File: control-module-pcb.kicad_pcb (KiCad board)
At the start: 4 copper layers, 59 x 75 mm, 79 parts, among them J1 Programming Header, J2 Programming Jumper, J3 Power Outputs, J4 Ignition Outputs, J5 Power Input, SW1 EN, U1 ESP32-S3-WROOM-1, U10 ITS4200SSJDXUMA1, U11 ITS4200SSJDXUMA1, U12 ITS4200SSJDXUMA1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

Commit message: layout mostly complete
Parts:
- added REF**: MountingHole_3.2mm_M3_ISO7380_Pad_TopBottom, MountingHole:MountingHole_3.2mm_M3_ISO7380_Pad_TopBottom, F.Cu at (171.5, 122.5)
- added REF**: MountingHole_3.2mm_M3_ISO7380_Pad_TopBottom, MountingHole:MountingHole_3.2mm_M3_ISO7380_Pad_TopBottom, F.Cu at (171.8, 64.5)
- moved R23 52.5 mm to (173.8, 77.1), turned to 180 degrees
- moved R24 52.2 mm to (173.8, 78.8)
- moved R25 51.9 mm to (173.8, 80.5), turned to 180 degrees
- moved R26 51.6 mm to (173.8, 82.2)
- moved J5 49.8 mm to (146.4, 128.6), turned to 90 degrees
- moved R2 31.6 mm to (145.3, 92.8), turned to 0 degrees
- moved SW1 27.6 mm to (162.8, 61.7), turned to -90 degrees
- moved J1 26.4 mm to (152.2, 67.1), turned to 90 degrees
- moved J2 18.8 mm to (144.7, 67.1), turned to 90 degrees
- moved U1 17.4 mm to (151.4, 82.1), turned to 90 degrees
- moved C2 7.39 mm to (146.9, 113.3), turned to 0 degrees
- moved C1A1 4.25 mm to (150.7, 108.4)
- moved C1B1 4.25 mm to (163.8, 108.3)
- moved C1C1 4.25 mm to (152.8, 108.3)
- moved C1D1 4.25 mm to (161.8, 108.2)
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- renumbered R25 to R24, R24 to R25
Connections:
- R23 pad 2: Net-(U1-GPIO1/TOUCH1/ADC1_CH0) -> Net-(U1-GPIO6/TOUCH6/ADC1_CH5)
- R24 pad 1: Net-(U1-GPIO1/TOUCH1/ADC1_CH0) -> Net-(U1-GPIO6/TOUCH6/ADC1_CH5)
- R25 pad 2: Net-(U1-GPIO2/TOUCH2/ADC1_CH1) -> Net-(U1-GPIO7/TOUCH7/ADC1_CH6)
- R26 pad 1: Net-(U1-GPIO2/TOUCH2/ADC1_CH1) -> Net-(U1-GPIO7/TOUCH7/ADC1_CH6)
- U1 pad 10: /R_BLIND_SPOT_ERR -> unconnected-(U1-GPIO17/U1TXD/ADC2_CH6-Pad10)
- U1 pad 11: /DASH_CAM_ERR -> /BACKUP_CAM_EN
- U1 pad 12: /HEAD_UNIT_EN -> /BACK_UP_CAM_ERR
- U1 pad 15: /IGNITION1_EN -> /DASH_CAM_EN
- U1 pad 16: /ACCESSORY1_ERR -> /DASH_CAM_ERR
- U1 pad 17: /L_BLIND_SPOT_EN -> /R_BLIND_SPOT_EN
- U1 pad 18: /R_BLIND_SPOT_EN -> /R_BLIND_SPOT_ERR
- U1 pad 19: /DASH_CAM_EN -> /L_BLIND_SPOT_EN
- U1 pad 20: /BACKUP_CAM_EN -> /L_BLIND_SPOT_ERR
- U1 pad 21: /HEAD_UNIT_ERR -> /HEAD_UNIT_EN
- U1 pad 22: /L_BLIND_SPOT_ERR -> /HEAD_UNIT_ERR
- U1 pad 23: /BACK_UP_CAM_ERR -> /STARTER_ERR
- U1 pad 24: /IGNITION2_ERR -> /STARTER_EN
- U1 pad 26: /IGNITION1_ERR -> /ACCESSORY2_EN
- U1 pad 28: unconnected-(U1-SPIIO6/GPIO35/FSPID/SUBSPID-Pad28) -> /IGNITION2_ERR
- U1 pad 29: unconnected-(U1-SPIIO7/GPIO36/FSPICLK/SUBSPICLK-Pad29) -> /IGNITION2_EN
- U1 pad 30: unconnected-(U1-SPIDQS/GPIO37/FSPIQ/SUBSPIQ-Pad30) -> /ACCESSORY1_ERR
- U1 pad 31: /STARTER_ERR -> /ACCESSORY1_EN
- U1 pad 38: Net-(U1-GPIO2/TOUCH2/ADC1_CH1) -> /IGNITION1_ERR
- U1 pad 39: Net-(U1-GPIO1/TOUCH1/ADC1_CH0) -> /IGNITION1_EN
- U1 pad 4: /ACCESSORY1_EN -> unconnected-(U1-GPIO4/TOUCH4/ADC1_CH3-Pad4)
- U1 pad 5: /IGNITION2_EN -> unconnected-(U1-GPIO5/TOUCH5/ADC1_CH4-Pad5)
- U1 pad 6: /ACCESSORY2_EN -> Net-(U1-GPIO6/TOUCH6/ADC1_CH5)
- U1 pad 7: /STARTER -> Net-(U1-GPIO7/TOUCH7/ADC1_CH6)
- U5 pad 3: /R_BLIND_SPOT_EN -> /L_BLIND_SPOT_EN
- U6 pad 3: /DASH_CAM_EN -> /R_BLIND_SPOT_EN
- U7 pad 3: /L_BLIND_SPOT_EN -> /DASH_CAM_EN
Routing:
- net /5V: track 52.1 -> 150.1 mm, vias 8 -> 24
- net /DASH_CAM_SHUTDOWN: track 0.00 -> 54.7 mm, vias 0 -> 2
- net /BACKUP_CAM_EN: track 0.00 -> 54.2 mm
- net /EN: track 0.00 -> 46.8 mm, vias 0 -> 2
- net /BACK_UP_CAM_ERR: track 5.95 -> 52.0 mm
- net /HEAD_UNIT_SHUTDOWN: track 0.00 -> 45.7 mm, vias 0 -> 2
- net /IGNITION1_EN: track 0.00 -> 44.7 mm
- net /DASH_CAM_EN: track 0.00 -> 43.8 mm
- net /IGNITION1_ERR: track 0.00 -> 40.8 mm
- net /DASH_CAM_ERR: track 5.93 -> 45.8 mm
- net /R_BLIND_SPOT_EN: track 0.00 -> 38.3 mm
- net /R_BLIND_SPOT_ERR: track 5.93 -> 40.0 mm
- net /L_BLIND_SPOT_EN: track 0.00 -> 32.4 mm
- net Net-(U1-GPIO6/TOUCH6/ADC1_CH5): track 0.00 -> 30.7 mm, vias 0 -> 2
- net /ACCESSORY1_EN: track 0.00 -> 29.3 mm
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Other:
- board size 59 x 75 mm -> 59 x 75.9 mm

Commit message: made a few adjustments and generated gerbers
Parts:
- moved C7 0.31 mm to (178.3, 93.7)
- moved C9 0.25 mm to (178.3, 102.0)
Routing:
- net /5V: track 150.1 -> 150.2 mm, vias 24 -> 26
- added copper zone on B.Cu, net GND
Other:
- board size 59 x 75.9 mm -> 58.2 x 75.9 mm
- board text added: "Ben Martens 2024-02"

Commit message: add LED for debugging
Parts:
- added D1: LED, LED_SMD:LED_0603_1608Metric, F.Cu at (168.6, 100.2)
- added R27: 220, Resistor_SMD:R_0603_1608Metric, F.Cu at (168.6, 98.4)
- R8: value 115 -> 145
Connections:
- U1 pad 5: unconnected-(U1-GPIO5/TOUCH5/ADC1_CH4-Pad5) -> Net-(U1-GPIO5/TOUCH5/ADC1_CH4)
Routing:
- net Net-(U1-GPIO5/TOUCH5/ADC1_CH4): track 0.00 -> 22.8 mm, vias 0 -> 2
- net Net-(D1-A): track 0.00 -> 1.76 mm
- net GND: vias 68 -> 69

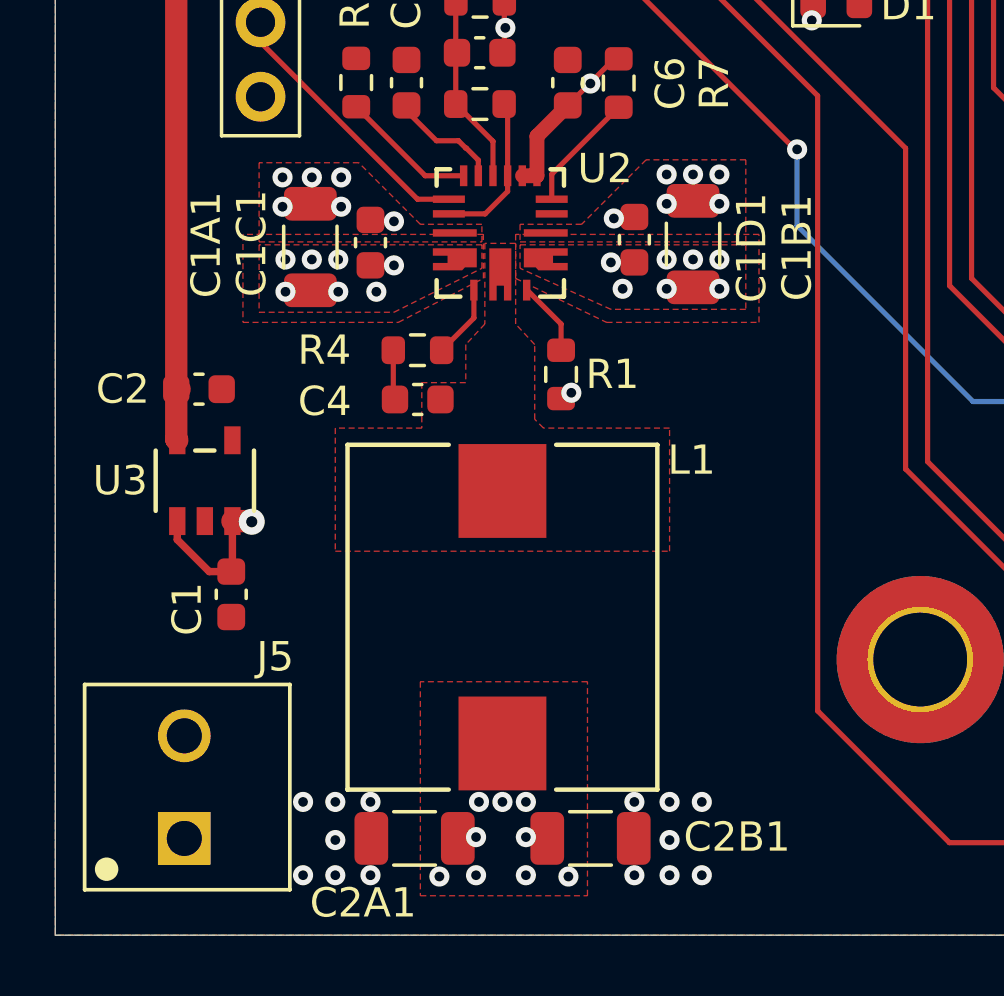
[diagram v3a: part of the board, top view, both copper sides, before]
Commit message: a few silk screen updates
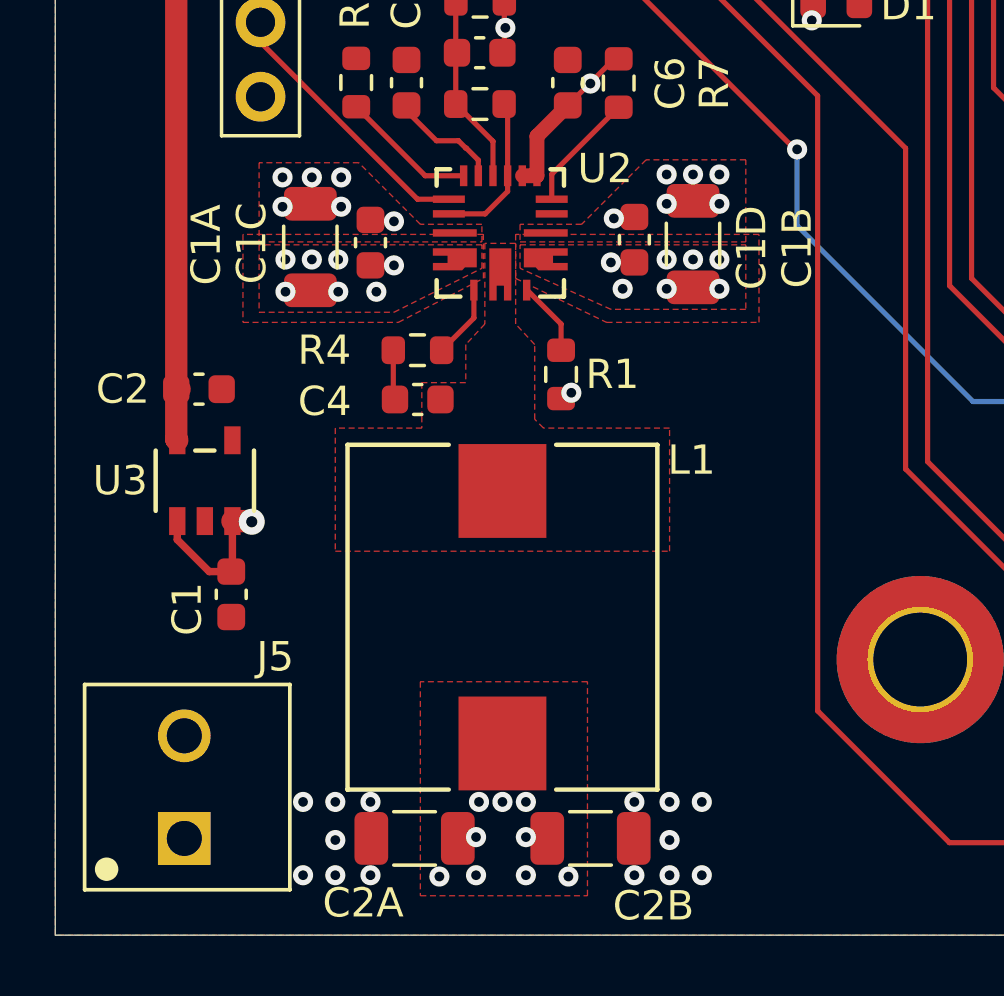
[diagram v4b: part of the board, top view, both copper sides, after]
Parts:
- renumbered C1A1 to C1A, C1B1 to C1B, C1C1 to C1C, C1D1 to C1D, C2A1 to C2A, C2B1 to C2B
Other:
- board text added: "Ben Martens 2024-02 Control Module v1"
- board text removed: "Ben Martens 2024-02"
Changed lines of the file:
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@@
         (effects (font (size 1 1) (thickness 0.15)))
     )
-    (fp_text value "4.7u" (at 0 0 90 unlocked) (layer "F.Fab")
+    (fp_text value "4.7u" (at -0.9447 6.25 90 unlocked) (layer "F.Fab")
         (effects (font (size 1 1) (thickness 0.15)))
     )
@@
     (zone_connect 2)
     (attr smd exclude_from_pos_files)
-    (fp_text reference "C2B1" (at 4.996867 -0.044389) (layer "F.SilkS")
+    (fp_text reference "C2B" (at 2.146867 2.300311) (layer "F.SilkS")
         (effects (font (size 1 1) (thickness 0.15)))
     )
@@
         (effects (font (size 1 1) (thickness 0.15)))
     )
-    (fp_text value "Programming Jumper" (at 8.525 4.975 90) (layer "F.Fab")
+    (fp_text value "Programming Jumper" (at 18.825 3.975 90) (layer "F.Fab")
         (effects (font (size 1 1) (thickness 0.15)))
     )
@@
     (property "ki_keywords" "cap capacitor")
     (attr smd exclude_from_pos_files)
-    (fp_text reference "C1B1" (at 0.125126 -3.551002 90) (layer "F.SilkS")
+    (fp_text reference "C1B" (at 0.125126 -3.551002 90) (layer "F.SilkS")
         (effects (font (size 1 1) (thickness 0.15)))
     )
@@
     (zone_connect 2)
     (attr smd exclude_from_pos_files)
-    (fp_text reference "C2A1" (at 1.753133 -2.200311 180) (layer "F.SilkS")
+    (fp_text reference "C2A" (at 1.753133 -2.200311 180) (layer "F.SilkS")
         (effects (font (size 1 1) (thickness 0.15)))
     )
@@
     (property "ki_keywords" "cap capacitor")
     (attr smd)
-    (fp_text reference "C1D1" (at 0.275 -4 90) (layer "F.SilkS")
+    (fp_text reference "C1D" (at 0.275 -4 90) (layer "F.SilkS")
         (effects (font (size 1 1) (thickness 0.15)))
     )
@@
         (effects (font (size 1 1) (thickness 0.15)))
     )
-    (fp_text value "Programming Header" (at 8.425 7.53 90) (layer "F.Fab")
+    (fp_text value "Programming Header" (at 18.625 6.23 90) (layer "F.Fab")
         (effects (font (size 1 1) (thickness 0.15)))
     )
@@
     (property "ki_keywords" "cap capacitor")
     (attr smd)
-    (fp_text reference "C1C1" (at 0.024874 4.051002 90) (layer "F.SilkS")
+    (fp_text reference "C1C" (at 0.024874 4.051002 90) (layer "F.SilkS")
         (effects (font (size 1 1) (thickness 0.15)))
     )
@@
     (property "ki_keywords" "cap capacitor")
     (attr smd exclude_from_pos_files)
-    (fp_text reference "C1A1" (at -0.075 3.55 90) (layer "F.SilkS")
+    (fp_text reference "C1A" (at -0.075 3.55 90) (layer "F.SilkS")
         (effects (font (size 1 1) (thickness 0.15)))
     )
@@
   (gr_rect (start 142 56) (end 200.25 131.9)
     (stroke (width 0.0381) (type default)) (fill none) (layer "Edge.Cuts"))
-  (gr_text "Ben Martens\n2024-02" (at 146.5 76.5 90) (layer "B.SilkS")
+  (gr_text "Ben Martens\n2024-02\nControl Module v1" (at 163 62.8) (layer "B.SilkS")
     (effects (font (size 1.25 1.25) (thickness 0.1524) bold) (justify left bottom mirror))
   )
